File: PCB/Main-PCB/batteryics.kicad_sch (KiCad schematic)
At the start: 2 parts, among them U2 BQ25188, U3 BQ27Z758

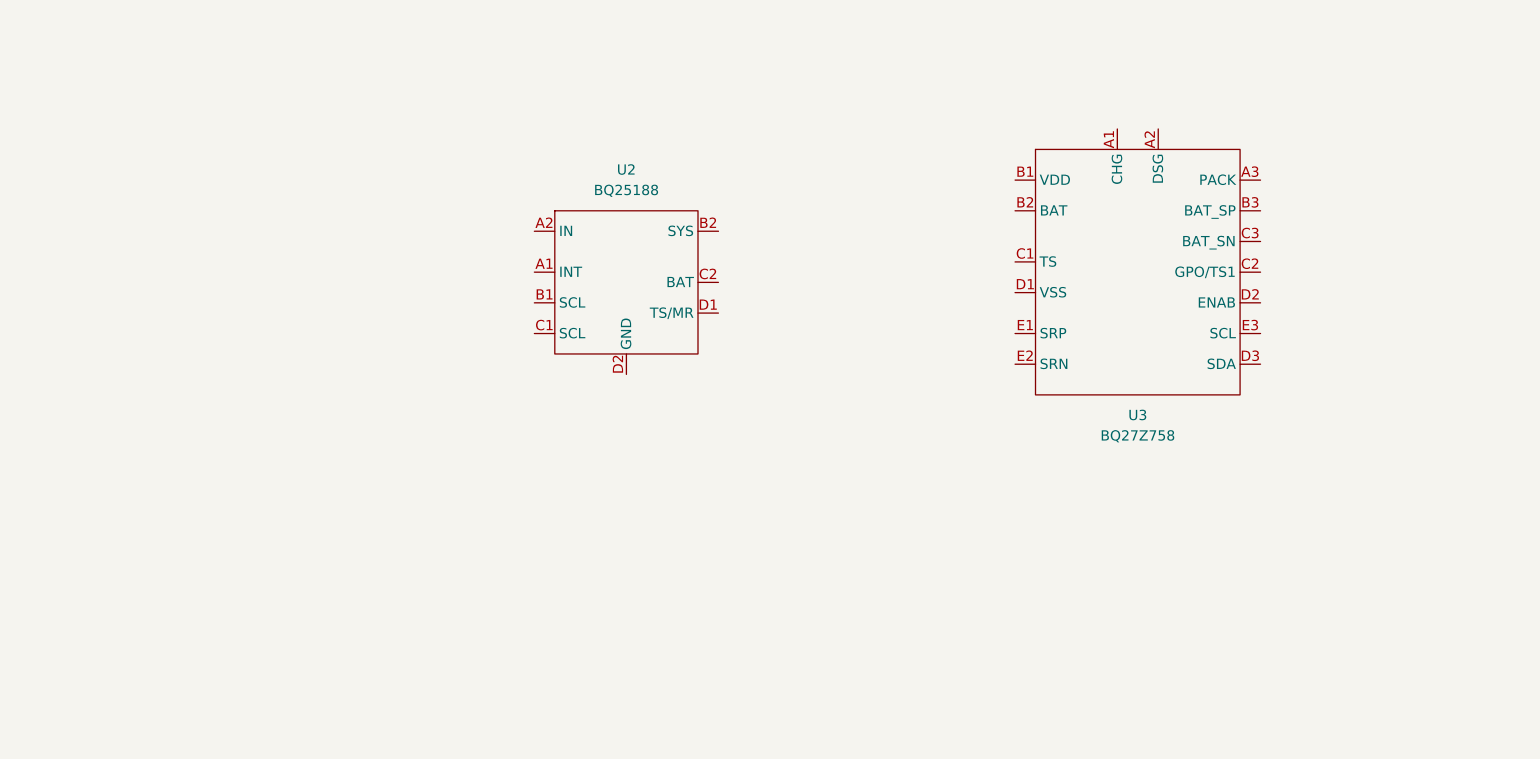
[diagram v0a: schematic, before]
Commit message: Finished schematic for SIM800C and power chips
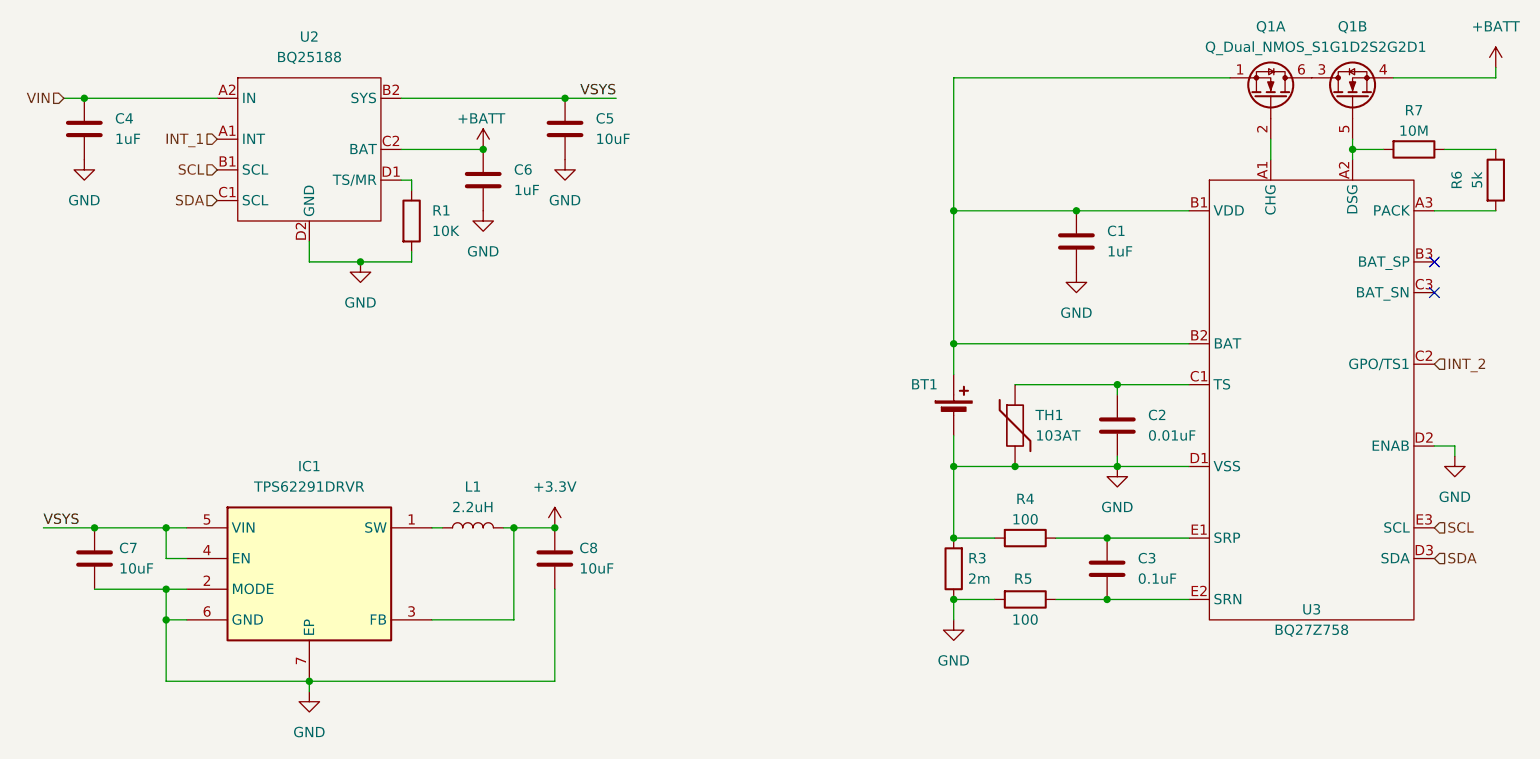
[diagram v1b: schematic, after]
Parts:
- added BT1: Battery_Cell, symbol Device:Battery_Cell
- added C1, C4, C6: 1uF, symbol Device:C
- added C2: 0.01uF, symbol Device:C
- added C3: 0.1uF, symbol Device:C
- added C5, C7, C8: 10uF, symbol Device:C
- added IC1: TPS62291DRVR, SON65P200X200X80-7N, symbol Components:TPS62291DRVR
- added L1: 2.2uH, symbol Device:L
- added Q1: Q_Dual_NMOS_S1G1D2S2G2D1, symbol Transistor_FET:Q_Dual_NMOS_S1G1D2S2G2D1
- added R1: 10K, symbol Device:R
- added R3: 2m, symbol Device:R
- added R4, R5: 100, symbol Device:R
- added R6: 5k, symbol Device:R
- added R7: 10M, symbol Device:R
- added TH1: 103AT, symbol Device:Thermistor
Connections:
- net at U3.A1 (CHG): now also Q1.2 (G)
- net at U3.A2 (DSG): now also Q1.5 (G), R7.2
- net at U3.A3 (PACK): now also R6.2
- net at U3.B1 (VDD): now also U3.B2 (BAT), BT1.1 (+), C1.1, Q1.1 (S)
- net at U3.C1 (TS): now also C2.1, TH1.1
- net INT_2: now reaches U3.C2 (GPO/TS1)
- net GND: now reaches U3.D1 (VSS)
- net GND: now also U2.D2 (GND), U3.D2 (ENAB), BT1.2 (-), C1.2, C2.2, C4.2, C5.2, C6.2, C7.2, C8.2, IC1.2 (MODE), IC1.6 (GND), IC1.7 (EP), R1.2, R3.1, R3.2, R4.2, R5.2, TH1.2
- net SDA: now reaches U3.D3 (SDA)
- net SDA: now also U2.C1 (SCL)
- net at U3.E1 (SRP): now also C3.1, R4.1
- net at U3.E2 (SRN): now also C3.2, R5.1
- net SCL: now reaches U3.E3 (SCL)
- net SCL: now also U2.B1 (SCL)
- net INT_1: now reaches U2.A1 (INT)
- net VIN: now reaches U2.A2 (IN)
- net VIN: now also C4.1
- net VSYS: now reaches U2.B2 (SYS)
- net VSYS: now also C5.1, C7.1, IC1.4 (EN), IC1.5 (VIN)
- net +BATT: now reaches U2.C2 (BAT)
- net +BATT: now also C6.1, Q1.4 (S)
- net at U2.D1 (TS/MR): now also R1.1
- new net: Q1.3 (D), Q1.6 (D)
- new net: IC1.1 (SW), L1.1
- new net: R6.1, R7.1
- new net +3.3V: C8.1, IC1.3 (FB), L1.2
- no-connect marks 0 -> 2
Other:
- moved on the sheet: U2

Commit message: Added MCU scheme
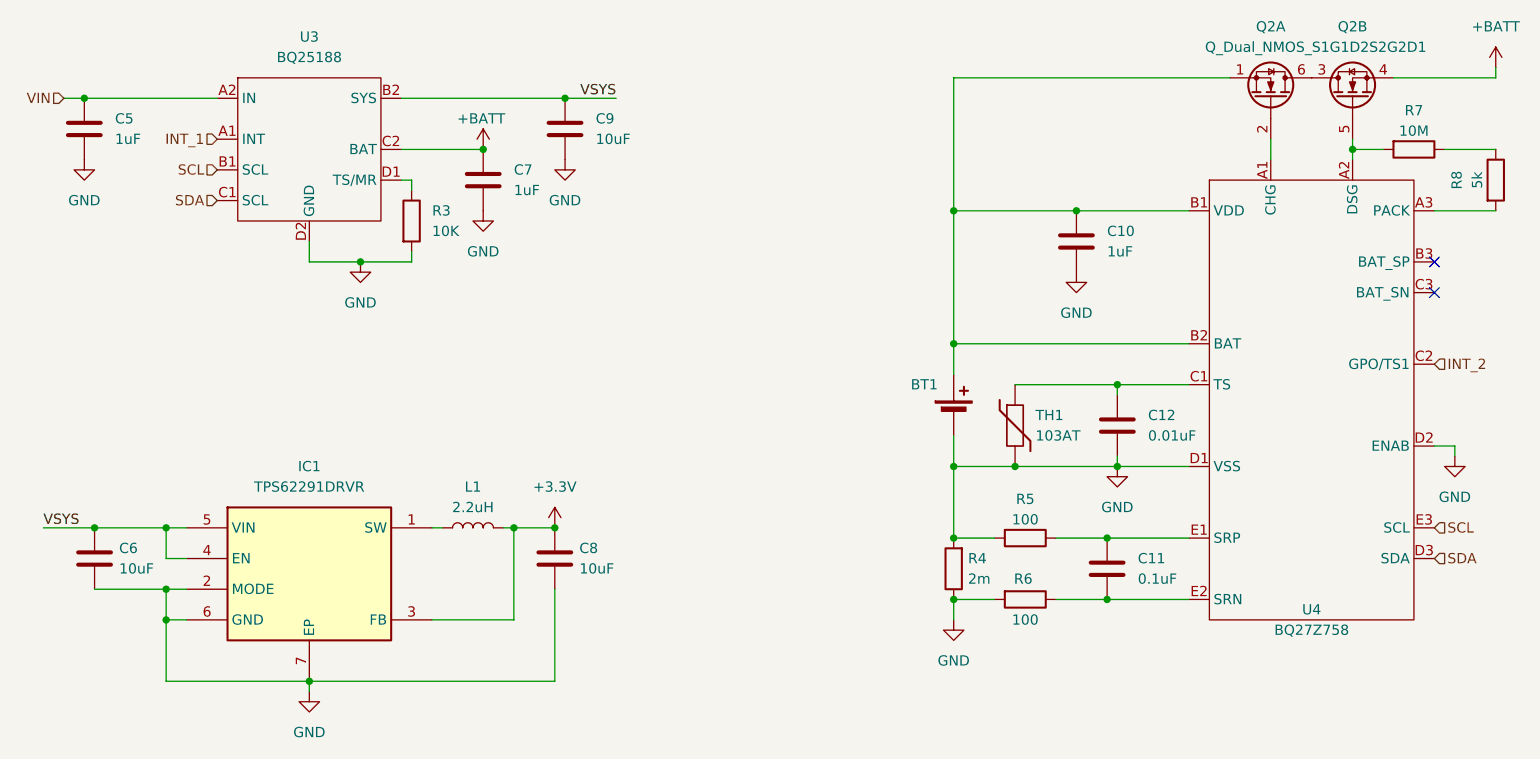
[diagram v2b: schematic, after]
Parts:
- renumbered C1 to C10, C3 to C11, C2 to C12, C4 to C5, C7 to C6, C6 to C7, C5 to C9, Q1 to Q2, R1 to R3, R3 to R4, R4 to R5, R5 to R6, R6 to R8, U2 to U3, U3 to U4
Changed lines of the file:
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@@
 		(dnp no)
 		(fields_autoplaced yes)
-		(property "Reference" "#PWR06"
+		(property "Reference" "#PWR013"
 			(at 151.13 124.46 0)
 			(effects
@@
 			(project "Main-PCB"
 				(path "/c7746b69-5ef2-4ca8-9a58-52c790d00466/161212a4-6ae2-4085-bd88-106b0438160b"
-					(reference "#PWR06")
+					(reference "#PWR013")
 					(unit 1)
 				)
@@
 		(dnp no)
 		(fields_autoplaced yes)
-		(property "Reference" "U3"
+		(property "Reference" "U4"
 			(at 195.58 116.84 0)
 			(effects
@@
 			(project ""
 				(path "/c7746b69-5ef2-4ca8-9a58-52c790d00466/161212a4-6ae2-4085-bd88-106b0438160b"
-					(reference "U3")
+					(reference "U4")
 					(unit 1)
 				)
@@
 		(on_board yes)
 		(dnp no)
-		(property "Reference" "R3"
+		(property "Reference" "R4"
 			(at 152.908 110.49 0)
 			(effects
@@
 			(project "Main-PCB"
 				(path "/c7746b69-5ef2-4ca8-9a58-52c790d00466/161212a4-6ae2-4085-bd88-106b0438160b"
-					(reference "R3")
+					(reference "R4")
 					(unit 1)
 				)
@@
 		(on_board yes)
 		(dnp no)
-		(property "Reference" "C7"
+		(property "Reference" "C6"
 			(at 47.498 109.22 0)
 			(effects
@@
 			(project ""
 				(path "/c7746b69-5ef2-4ca8-9a58-52c790d00466/161212a4-6ae2-4085-bd88-106b0438160b"
-					(reference "C7")
+					(reference "C6")
 					(unit 1)
 				)
@@
 		(on_board yes)
 		(dnp no)
-		(property "Reference" "#PWR08"
+		(property "Reference" "#PWR09"
 			(at 92.71 63.5 0)
 			(effects
@@
 			(project "Main-PCB"
 				(path "/c7746b69-5ef2-4ca8-9a58-52c790d00466/161212a4-6ae2-4085-bd88-106b0438160b"
-					(reference "#PWR08")
+					(reference "#PWR09")
 					(unit 1)
 				)
@@
 		(dnp no)
 		(fields_autoplaced yes)
-		(property "Reference" "R1"
+		(property "Reference" "R3"
 			(at 86.36 67.3099 0)
 			(effects
@@
 			(project ""
 				(path "/c7746b69-5ef2-4ca8-9a58-52c790d00466/161212a4-6ae2-4085-bd88-106b0438160b"
-					(reference "R1")
+					(reference "R3")
 					(unit 1)
 				)
@@
 		(dnp no)
 		(fields_autoplaced yes)
-		(property "Reference" "#PWR010"
+		(property "Reference" "#PWR012"
 			(at 102.87 67.31 0)
 			(effects
@@
 			(project "Main-PCB"
 				(path "/c7746b69-5ef2-4ca8-9a58-52c790d00466/161212a4-6ae2-4085-bd88-106b0438160b"
-					(reference "#PWR010")
+					(reference "#PWR012")
 					(unit 1)
 				)
@@
 		(on_board yes)
 		(dnp no)
-		(property "Reference" "Q1"
+		(property "Reference" "Q2"
 			(at 190.5 44.45 90)
 			(effects
@@
 			(project ""
 				(path "/c7746b69-5ef2-4ca8-9a58-52c790d00466/161212a4-6ae2-4085-bd88-106b0438160b"
-					(reference "Q1")
+					(reference "Q2")
 					(unit 1)
 				)
@@
 		(dnp no)
 		(fields_autoplaced yes)
-		(property "Reference" "#PWR02"
+		(property "Reference" "#PWR014"
 			(at 166.37 81.28 0)
 			(effects
@@
 			(project ""
 				(path "/c7746b69-5ef2-4ca8-9a58-52c790d00466/161212a4-6ae2-4085-bd88-106b0438160b"
-					(reference "#PWR02")
+					(reference "#PWR014")
 					(unit 1)
 				)
@@
 		(dnp no)
 		(fields_autoplaced yes)
-		(property "Reference" "#PWR09"
+		(property "Reference" "#PWR06"
 			(at 43.18 67.31 0)
 			(effects
@@
 			(project "Main-PCB"
 				(path "/c7746b69-5ef2-4ca8-9a58-52c790d00466/161212a4-6ae2-4085-bd88-106b0438160b"
-					(reference "#PWR09")
+					(reference "#PWR06")
 					(unit 1)
 				)
@@
 		(on_board yes)
 		(dnp no)
-		(property "Reference" "Q1"
+		(property "Reference" "Q2"
 			(at 200.66 44.45 90)
 			(effects
@@
 			(project ""
 				(path "/c7746b69-5ef2-4ca8-9a58-52c790d00466/161212a4-6ae2-4085-bd88-106b0438160b"
-					(reference "Q1")
+					(reference "Q2")
 					(unit 2)
 				)
@@
 		(dnp no)
 		(fields_autoplaced yes)
-		(property "Reference" "C4"
+		(property "Reference" "C5"
 			(at 46.99 55.8799 0)
 			(effects
@@
 			(project "Main-PCB"
 				(path "/c7746b69-5ef2-4ca8-9a58-52c790d00466/161212a4-6ae2-4085-bd88-106b0438160b"
-					(reference "C4")
+					(reference "C5")
 					(unit 1)
 				)
@@
 		(on_board yes)
 		(dnp no)
-		(property "Reference" "R6"
+		(property "Reference" "R8"
 			(at 213.614 63.5 90)
 			(effects
@@
 			(project "Main-PCB"
 				(path "/c7746b69-5ef2-4ca8-9a58-52c790d00466/161212a4-6ae2-4085-bd88-106b0438160b"
-					(reference "R6")
+					(reference "R8")
 					(unit 1)
 				)
@@
 		(dnp no)
 		(fields_autoplaced yes)
-		(property "Reference" "#PWR013"
+		(property "Reference" "#PWR011"
 			(at 101.6 110.49 0)
 			(effects
@@
 			(project ""
 				(path "/c7746b69-5ef2-4ca8-9a58-52c790d00466/161212a4-6ae2-4085-bd88-106b0438160b"
-					(reference "#PWR013")
+					(reference "#PWR011")
 					(unit 1)
 				)
@@
 		(on_board yes)
 		(dnp no)
-		(property "Reference" "R4"
+		(property "Reference" "R5"
 			(at 160.02 103.124 90)
 			(effects
@@
 			(project "Main-PCB"
 				(path "/c7746b69-5ef2-4ca8-9a58-52c790d00466/161212a4-6ae2-4085-bd88-106b0438160b"
-					(reference "R4")
+					(reference "R5")
 					(unit 1)
 				)
@@
 		(dnp no)
 		(fields_autoplaced yes)
-		(property "Reference" "#PWR012"
+		(property "Reference" "#PWR07"
 			(at 71.12 133.35 0)
 			(effects
@@
 			(project "Main-PCB"
 				(path "/c7746b69-5ef2-4ca8-9a58-52c790d00466/161212a4-6ae2-4085-bd88-106b0438160b"
-					(reference "#PWR012")
+					(reference "#PWR07")
 					(unit 1)
 				)
@@
 		(dnp no)
 		(fields_autoplaced yes)
-		(property "Reference" "#PWR03"
+		(property "Reference" "#PWR015"
 			(at 171.45 105.41 0)
 			(effects
@@
 			(project ""
 				(path "/c7746b69-5ef2-4ca8-9a58-52c790d00466/161212a4-6ae2-4085-bd88-106b0438160b"
-					(reference "#PWR03")
+					(reference "#PWR015")
 					(unit 1)
 				)
@@
 		(dnp no)
 		(fields_autoplaced yes)
-		(property "Reference" "#PWR07"
+		(property "Reference" "#PWR017"
 			(at 218.44 53.34 0)
 			(effects
@@
 			(project ""
 				(path "/c7746b69-5ef2-4ca8-9a58-52c790d00466/161212a4-6ae2-4085-bd88-106b0438160b"
-					(reference "#PWR07")
+					(reference "#PWR017")
 					(unit 1)
 				)
@@
 		(dnp no)
 		(fields_autoplaced yes)
-		(property "Reference" "C1"
+		(property "Reference" "C10"
 			(at 170.18 69.8499 0)
 			(effects
@@
 			(project ""
 				(path "/c7746b69-5ef2-4ca8-9a58-52c790d00466/161212a4-6ae2-4085-bd88-106b0438160b"
-					(reference "C1")
+					(reference "C10")
 					(unit 1)
 				)
@@
 		(dnp no)
 		(fields_autoplaced yes)
-		(property "Reference" "C3"
+		(property "Reference" "C11"
 			(at 173.99 110.4899 0)
 			(effects
@@
 			(project "Main-PCB"
 				(path "/c7746b69-5ef2-4ca8-9a58-52c790d00466/161212a4-6ae2-4085-bd88-106b0438160b"
-					(reference "C3")
+					(reference "C11")
 					(unit 1)
 				)
@@
 		(dnp no)
 		(fields_autoplaced yes)
-		(property "Reference" "C2"
+		(property "Reference" "C12"
 			(at 175.26 92.7099 0)
 			(effects
@@
 			(project "Main-PCB"
 				(path "/c7746b69-5ef2-4ca8-9a58-52c790d00466/161212a4-6ae2-4085-bd88-106b0438160b"
-					(reference "C2")
+					(reference "C12")
 					(unit 1)
 				)
@@
 		(dnp no)
 		(fields_autoplaced yes)
-		(property "Reference" "U2"
+		(property "Reference" "U3"
 			(at 71.12 45.72 0)
 			(effects
@@
 			(project ""
 				(path "/c7746b69-5ef2-4ca8-9a58-52c790d00466/161212a4-6ae2-4085-bd88-106b0438160b"
-					(reference "U2")
+					(reference "U3")
 					(unit 1)
 				)
@@
 		(dnp no)
 		(fields_autoplaced yes)
-		(property "Reference" "#PWR04"
+		(property "Reference" "#PWR016"
 			(at 213.36 104.14 0)
 			(effects
@@
 			(project ""
 				(path "/c7746b69-5ef2-4ca8-9a58-52c790d00466/161212a4-6ae2-4085-bd88-106b0438160b"
-					(reference "#PWR04")
+					(reference "#PWR016")
 					(unit 1)
 				)
@@
 		(dnp no)
 		(fields_autoplaced yes)
-		(property "Reference" "#PWR011"
+		(property "Reference" "#PWR010"
 			(at 92.71 73.66 0)
 			(effects
@@
 			(project "Main-PCB"
 				(path "/c7746b69-5ef2-4ca8-9a58-52c790d00466/161212a4-6ae2-4085-bd88-106b0438160b"
-					(reference "#PWR011")
+					(reference "#PWR010")
 					(unit 1)
 				)
@@
 		(on_board yes)
 		(dnp no)
-		(property "Reference" "R5"
+		(property "Reference" "R6"
 			(at 159.766 113.03 90)
 			(effects
@@
 			(project "Main-PCB"
 				(path "/c7746b69-5ef2-4ca8-9a58-52c790d00466/161212a4-6ae2-4085-bd88-106b0438160b"
-					(reference "R5")
+					(reference "R6")
 					(unit 1)
 				)
@@
 		(dnp no)
 		(fields_autoplaced yes)
-		(property "Reference" "C6"
+		(property "Reference" "C7"
 			(at 96.52 62.2299 0)
 			(effects
@@
 			(project "Main-PCB"
 				(path "/c7746b69-5ef2-4ca8-9a58-52c790d00466/161212a4-6ae2-4085-bd88-106b0438160b"
-					(reference "C6")
+					(reference "C7")
 					(unit 1)
 				)
@@
 		(dnp no)
 		(fields_autoplaced yes)
-		(property "Reference" "#PWR05"
+		(property "Reference" "#PWR08"
 			(at 77.47 80.01 0)
 			(effects
@@
 			(project ""
 				(path "/c7746b69-5ef2-4ca8-9a58-52c790d00466/161212a4-6ae2-4085-bd88-106b0438160b"
-					(reference "#PWR05")
+					(reference "#PWR08")
 					(unit 1)
 				)
@@
 		(dnp no)
 		(fields_autoplaced yes)
-		(property "Reference" "C5"
+		(property "Reference" "C9"
 			(at 106.68 55.8799 0)
 			(effects
@@
 			(project "Main-PCB"
 				(path "/c7746b69-5ef2-4ca8-9a58-52c790d00466/161212a4-6ae2-4085-bd88-106b0438160b"
-					(reference "C5")
-					(unit 1)
-				)
+					(reference "C9")
+					(unit 1)
+				)
